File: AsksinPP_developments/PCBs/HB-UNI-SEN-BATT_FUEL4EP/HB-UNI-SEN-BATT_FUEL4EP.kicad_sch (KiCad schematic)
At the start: 29 parts, among them J1 Conn_01x02, J10 charge, J2 Conn_01x02, J3 Conn_01x02, J4 Conn_01x02, J5 ISP Programmer, J6 Conn_01x04, J7 Conn_01x04, J8 Conn_01x04, J9 Conn_01x04, Q1 IRLU024N, SW1 config button

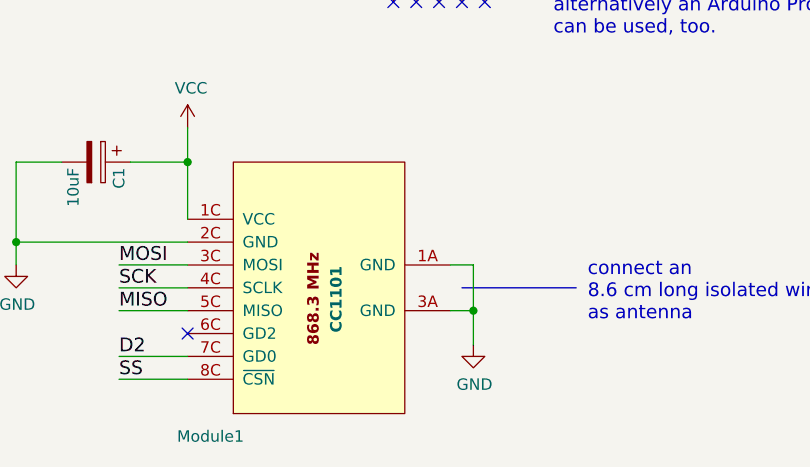
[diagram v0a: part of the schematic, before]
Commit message: PCBs: KiCAD6 required improvements of layout data bases; added E07-900M10S into FUEL and footprint library
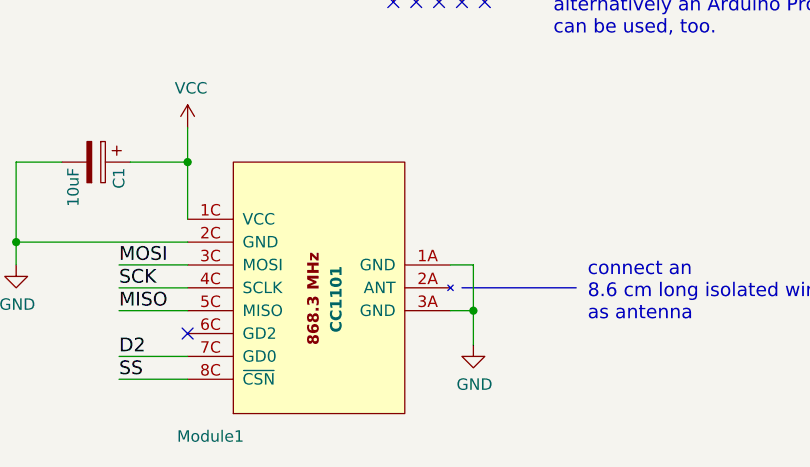
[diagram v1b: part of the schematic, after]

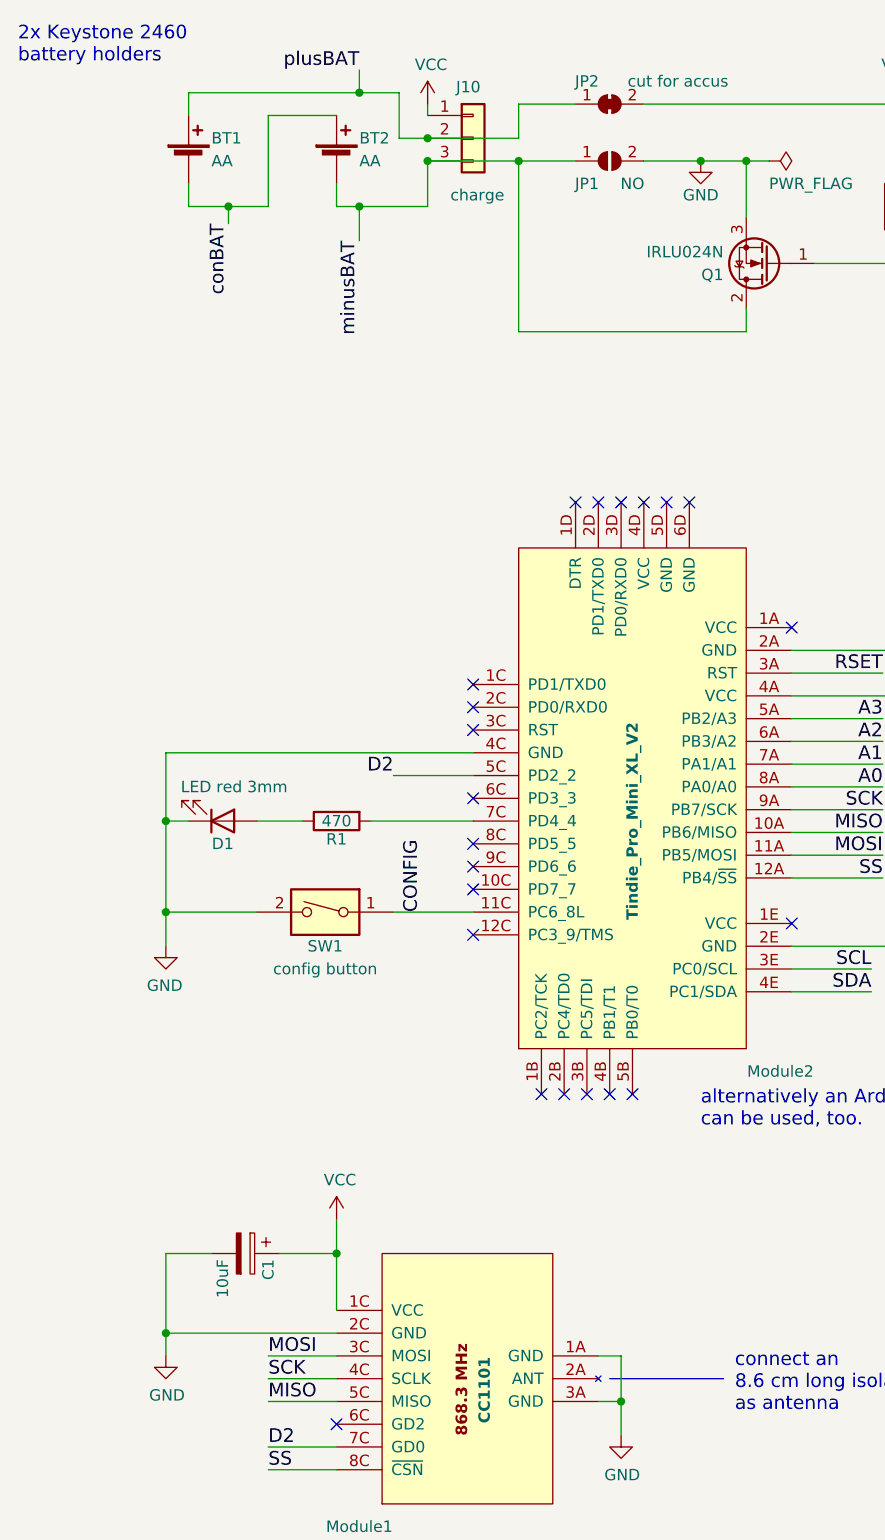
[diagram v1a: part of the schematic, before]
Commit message: PCBs/HB-UNI-SEN-BATT_FUEL4EP: migration to KiCAD 8
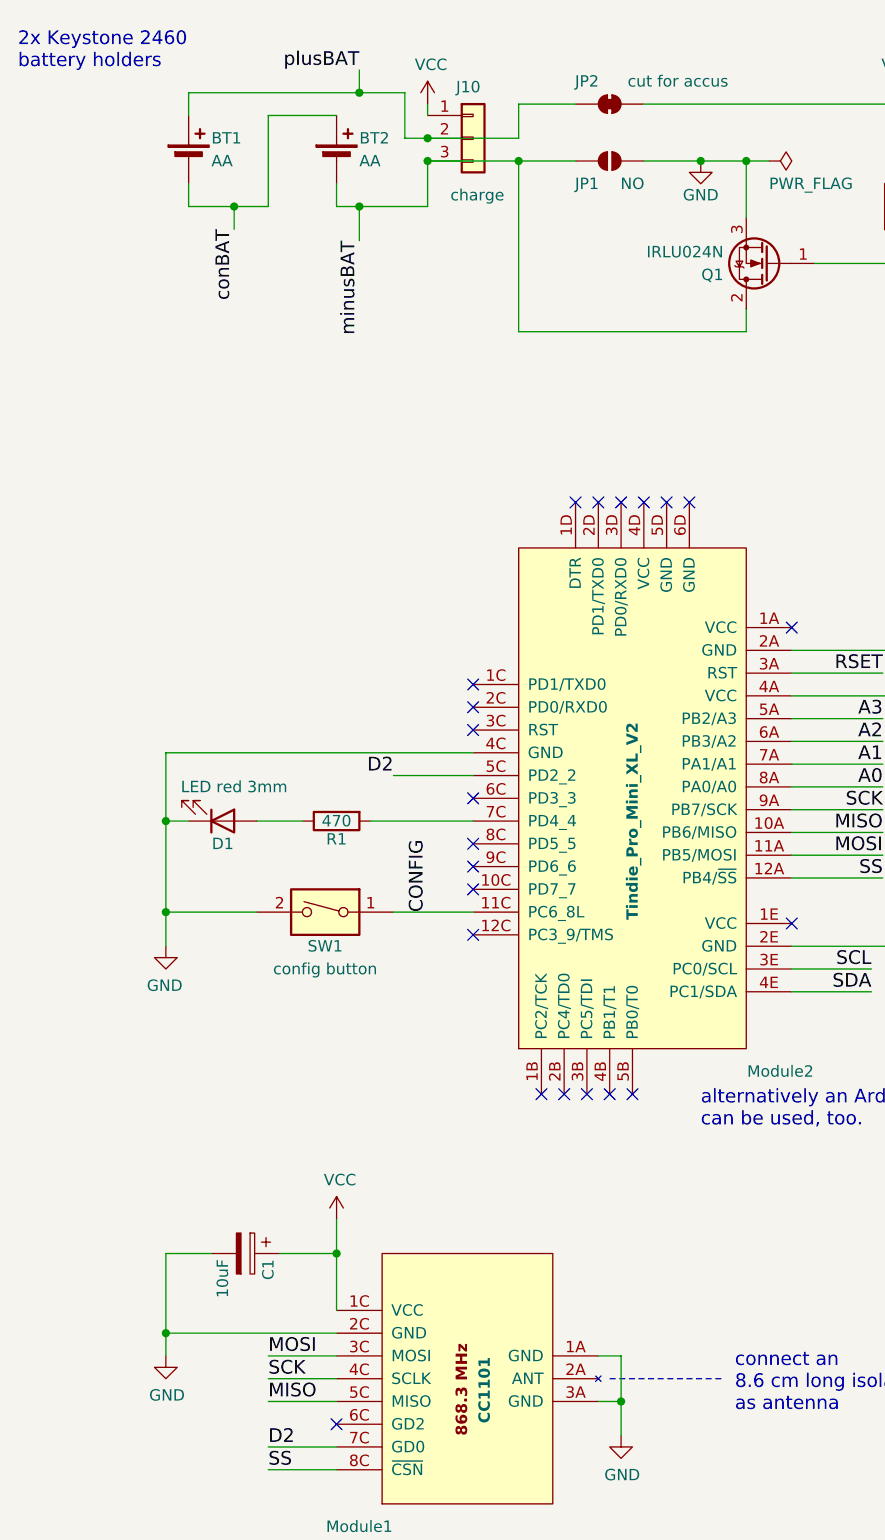
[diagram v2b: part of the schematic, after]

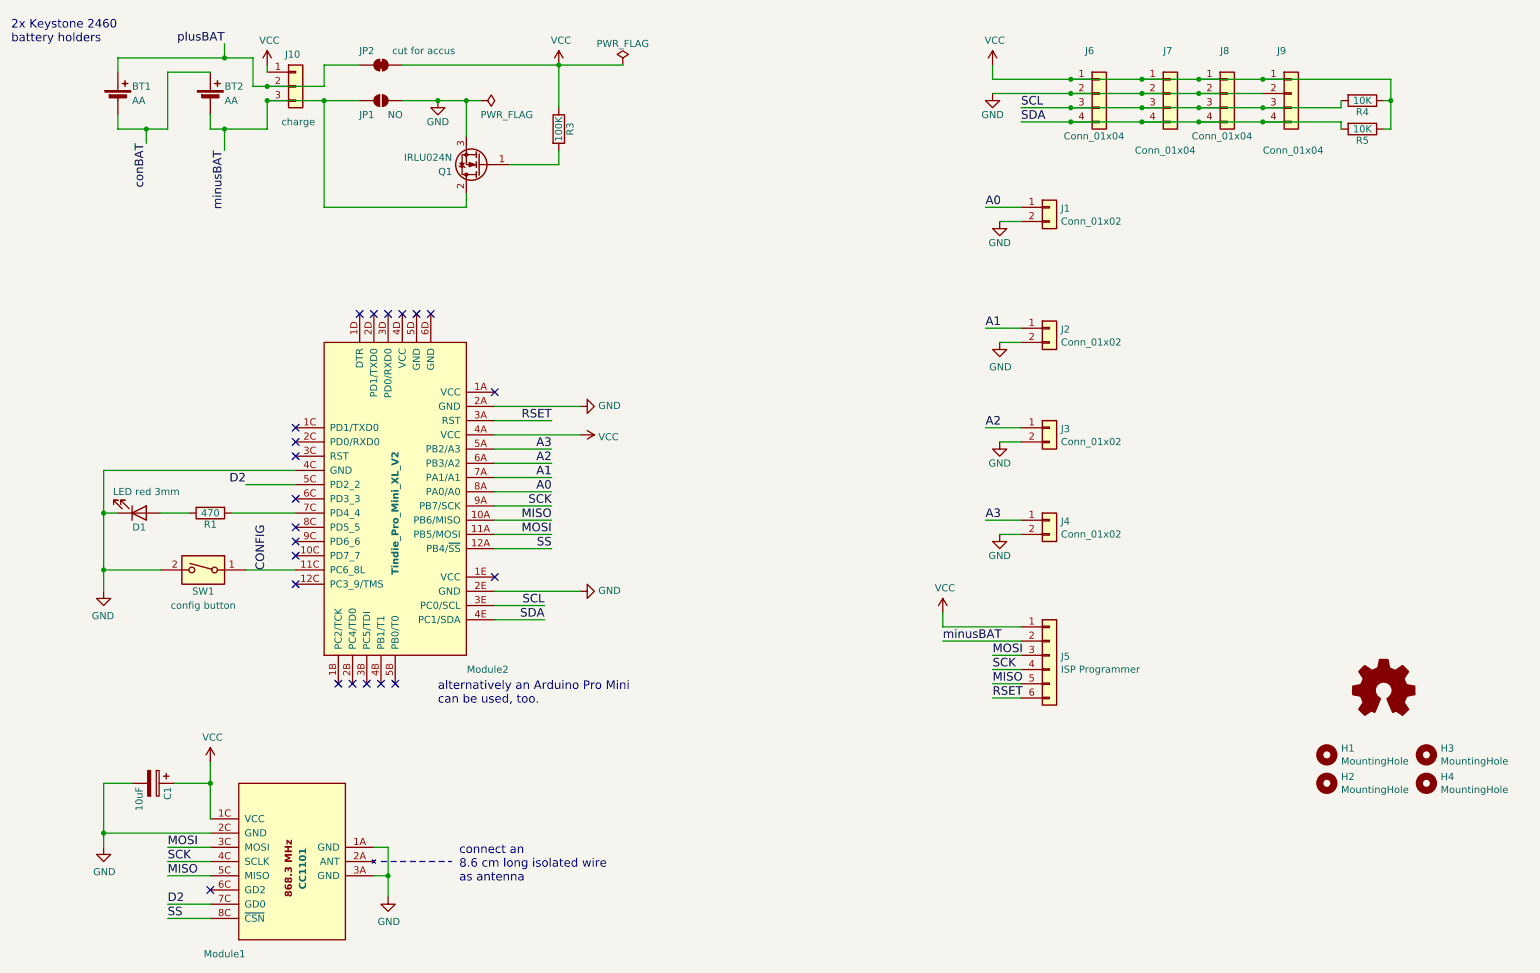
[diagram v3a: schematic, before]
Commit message: upgraded PCBs/HB-UNI-SEN-BATT_FUEL4EP to V1.5 supporting now HB_Pro_Mini_ATMEGA1284P_FUEL4EP
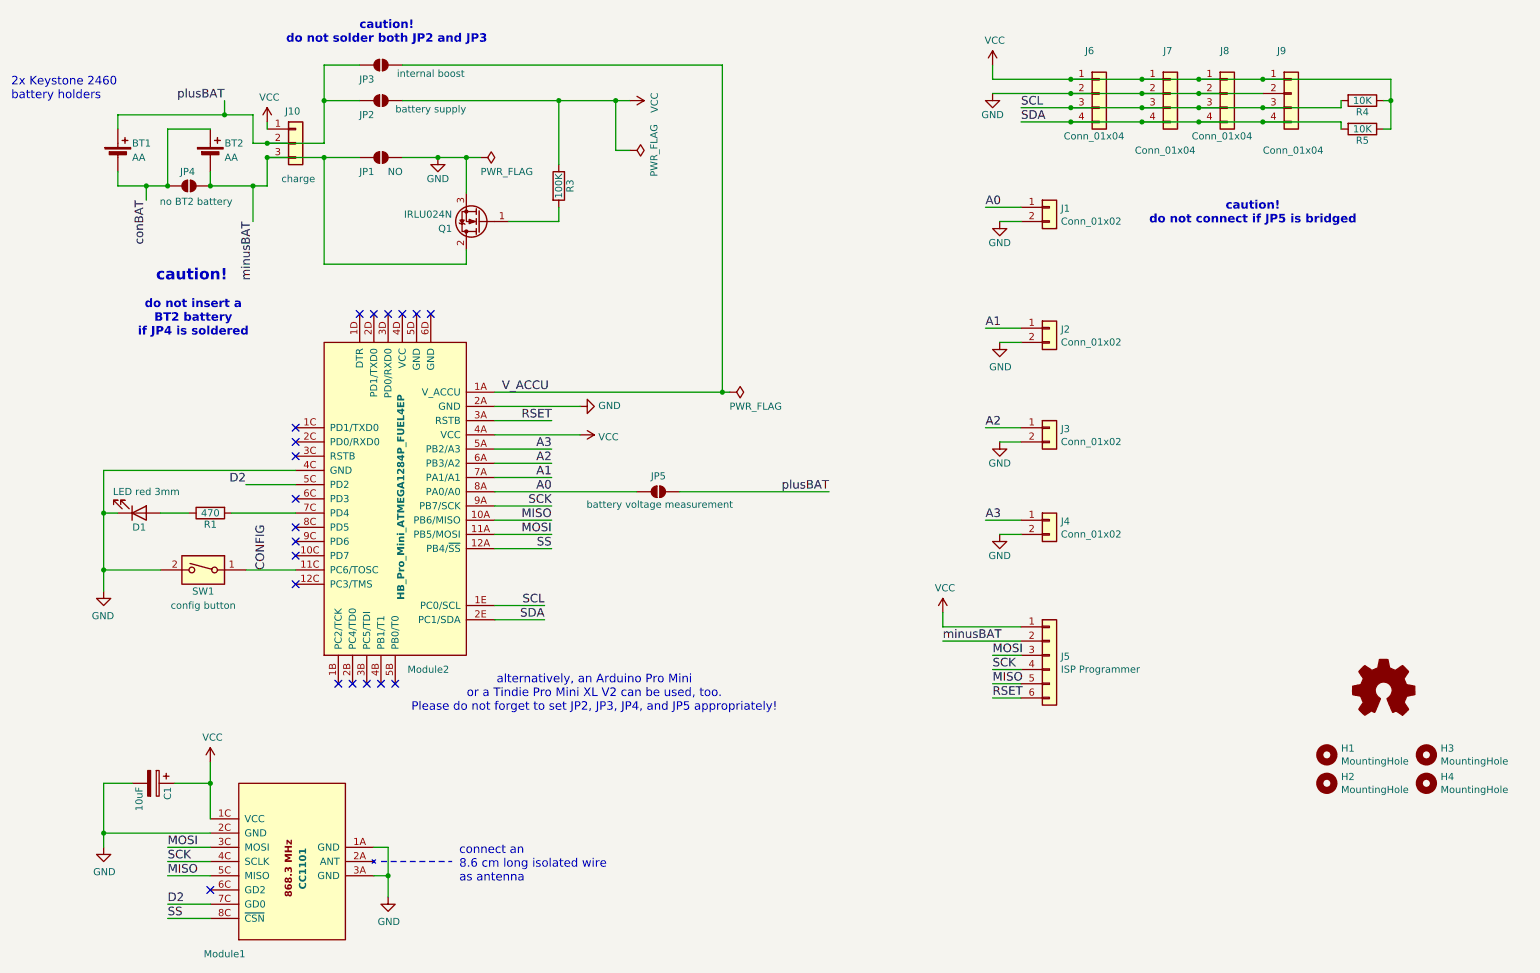
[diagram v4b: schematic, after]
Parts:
- removed JP2: cut for accus, Jumper:SolderJumper-2_P1.3mm_Bridged_Pad1.0x1.5mm, symbol Jumper:SolderJumper_2_Bridged
- removed Module2: Tindie_Pro_Mini_XL_V2, FUEL4EP:Tindie_ArduinoProMiniXL_1284P_V2, symbol FUEL4EP:Tindie_Pro_Mini_XL_V2
- added JP2: battery supply, Jumper:SolderJumper-2_P1.3mm_Open_Pad1.0x1.5mm, symbol Jumper:SolderJumper_2_Open
- added JP3: internal boost, Jumper:SolderJumper-2_P1.3mm_Open_Pad1.0x1.5mm, symbol Jumper:SolderJumper_2_Open
- added JP4: no BT2 battery, FUEL4EP:SolderJumper-2_P1.3mm_Open_Pad1.0x1.5mm, symbol Jumper:SolderJumper_2_Open
- added JP5: battery voltage measurement, Jumper:SolderJumper-2_P1.3mm_Open_Pad1.0x1.5mm, symbol Jumper:SolderJumper_2_Open
- added Module2: HB_Pro_Mini_ATMEGA1284P_FUEL4EP, FUEL4EP:HB_Pro_Mini_ATMEGA1284P_FUEL4EP, symbol FUEL4EP:HB_Pro_Mini_ATMEGA1284P_FUEL4EP
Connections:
- net A0: now also JP5.1 (A), Module2.8A (PA0/A0)
- net A1: now also Module2.7A (PA1/A1)
- net A2: now also Module2.6A (PB3/A2)
- net A3: now also Module2.5A (PB2/A3)
- net CONFIG: now also Module2.11C (PC6/TOSC)
- net D2: now also Module2.5C (PD2)
- net GND: now also Module2.2A (GND), Module2.4C (GND)
- net MISO: now also Module2.10A (PB6/MISO)
- net MOSI: now also Module2.11A (PB5/MOSI)
- net RSET: now also Module2.3A (RSTB)
- net SCK: now also Module2.9A (PB7/SCK)
- net SCL: now also Module2.1E (PC0/SCL)
- net SDA: now also Module2.2E (PC1/SDA)
- net SS: now also Module2.12A (PB4/~{SS})
- net VCC: now also JP2.2 (B), Module2.4A (VCC)
- net conBAT: now also JP4.1 (A)
- net minusBAT: now also JP4.2 (B)
- net plusBAT: now also JP2.1 (A), JP3.1 (A), JP5.2 (B)
- net at R1.2: now also Module2.7C (PD4)
- new net V_ACCU: JP3.2 (B), Module2.1A (V_ACCU)
- no-connect marks 22 -> 20
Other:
- note added: "alternatively, an Arduino Pro Mini or a Tindie Pro Mini XL V2 can be used, too. Please do not forget to set JP2, JP3, JP4, and JP5 appropriately!"
- note added: "caution!"
- note added: "caution! do not connect if JP5 is bridged"
- note added: "caution! do not solder both JP2 and JP3"
- note added: "do not insert a BT2 battery if JP4 is soldered"
- note removed: "alternatively an Arduino Pro Mini can be used, too."
- moved on the sheet: BT1, BT2, J10, JP1, Q1, R3
